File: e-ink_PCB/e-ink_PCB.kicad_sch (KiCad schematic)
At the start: 10 parts, among them J1 SEED C3, J2 e-ink-display, J3 SHT31, J4 100 uF CAP, J5 Batt Conn, Q1 FQP27P06

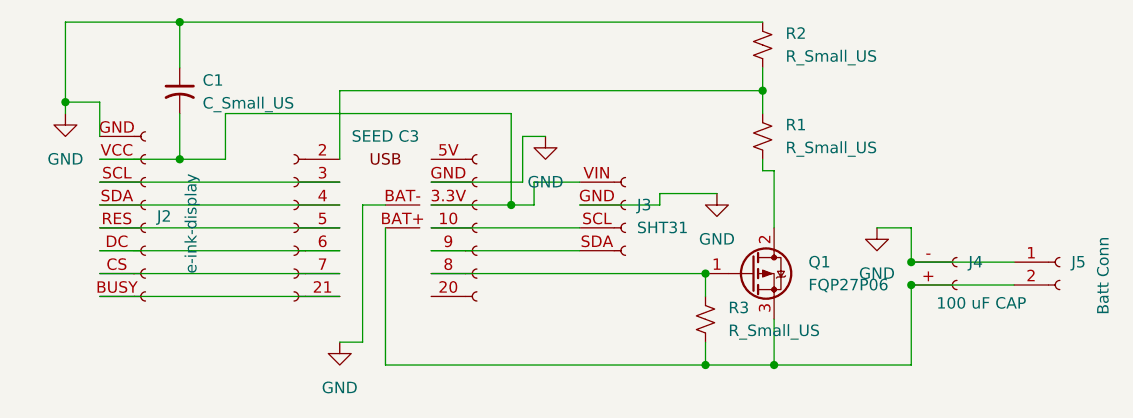
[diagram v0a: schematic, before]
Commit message: kiCAD correct display orientation
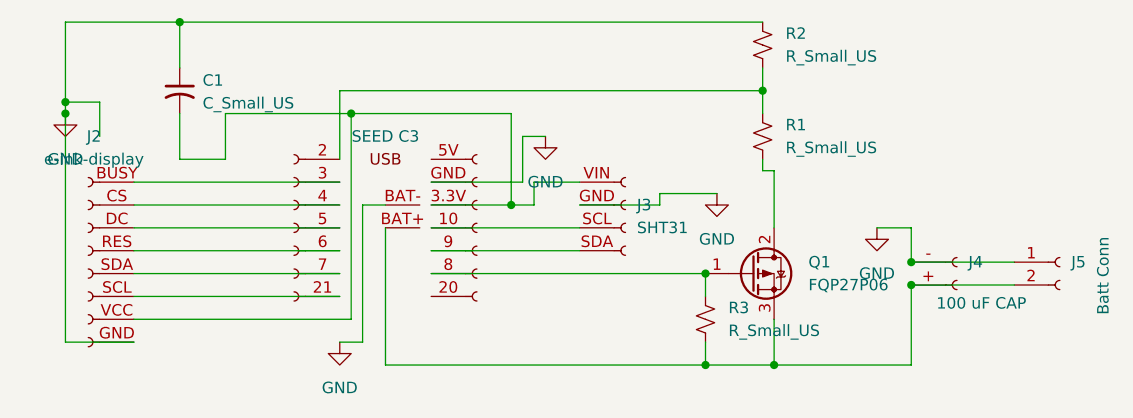
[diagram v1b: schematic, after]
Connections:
- net at J2.BUSY (Pin_8): now also J1.3 (Pin_7); no longer J1.21 (Pin_2)
- net at J2.CS (Pin_7): now also J1.4 (Pin_6); no longer J1.7 (Pin_3)
- net at J2.DC (Pin_6): now also J1.5 (Pin_5); no longer J1.6 (Pin_4)
- net at J2.RES (Pin_5): now also J1.6 (Pin_4); no longer J1.5 (Pin_5)
- net at J2.SCL (Pin_3): now also J1.21 (Pin_2); no longer J1.3 (Pin_7)
- net at J2.SDA (Pin_4): now also J1.7 (Pin_3); no longer J1.4 (Pin_6)
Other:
- moved on the sheet: J2
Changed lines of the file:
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@@
 	)
 	(junction
-		(at 72.39 72.39)
+		(at 91.44 67.31)
 		(diameter 0)
 		(color 0 0 0 0)
@@
 		(color 0 0 0 0)
 	)
-	(wire
-		(pts
-			(xy 77.47 72.39) (xy 72.39 72.39)
-		)
-		(stroke
-			(width 0)
-			(type default)
-		)
+	(junction
+		(at 59.69 67.31)
+		(diameter 0)
+		(color 0 0 0 0)
 	)
 	(wire
@@
 	(wire
 		(pts
+			(xy 67.31 85.09) (xy 90.17 85.09)
+		)
+		(stroke
+			(width 0)
+			(type default)
+		)
+	)
+	(wire
+		(pts
 			(xy 100.33 80.01) (xy 116.84 80.01)
 		)
@@
 	(wire
 		(pts
-			(xy 63.5 82.55) (xy 90.17 82.55)
+			(xy 72.39 72.39) (xy 77.47 72.39)
 		)
 		(stroke
@@
 	(wire
 		(pts
-			(xy 63.5 87.63) (xy 90.17 87.63)
+			(xy 67.31 87.63) (xy 90.17 87.63)
 		)
 		(stroke
@@
 	(wire
 		(pts
-			(xy 72.39 72.39) (xy 63.5 72.39)
+			(xy 67.31 82.55) (xy 90.17 82.55)
+		)
+		(stroke
+			(width 0)
+			(type default)
+		)
+	)
+	(wire
+		(pts
+			(xy 59.69 67.31) (xy 59.69 92.71)
+		)
+		(stroke
+			(width 0)
+			(type default)
+		)
+	)
+	(wire
+		(pts
+			(xy 67.31 92.71) (xy 59.69 92.71)
+		)
+		(stroke
+			(width 0)
+			(type default)
+		)
+	)
+	(wire
+		(pts
+			(xy 67.31 77.47) (xy 90.17 77.47)
 		)
 		(stroke
@@
 	(wire
 		(pts
+			(xy 91.44 67.31) (xy 77.47 67.31)
+		)
+		(stroke
+			(width 0)
+			(type default)
+		)
+	)
+	(wire
+		(pts
 			(xy 153.67 83.82) (xy 153.67 80.01)
 		)
@@
 	(wire
 		(pts
-			(xy 63.5 85.09) (xy 90.17 85.09)
-		)
-		(stroke
-			(width 0)
-			(type default)
-		)
-	)
-	(wire
-		(pts
 			(xy 100.33 85.09) (xy 130.81 85.09)
 		)
@@
 	(wire
 		(pts
+			(xy 67.31 74.93) (xy 90.17 74.93)
+		)
+		(stroke
+			(width 0)
+			(type default)
+		)
+	)
+	(wire
+		(pts
 			(xy 137.16 64.77) (xy 137.16 67.31)
 		)
@@
 	(wire
 		(pts
-			(xy 63.5 77.47) (xy 90.17 77.47)
-		)
-		(stroke
-			(width 0)
-			(type default)
-		)
-	)
-	(wire
-		(pts
-			(xy 109.22 67.31) (xy 77.47 67.31)
+			(xy 109.22 67.31) (xy 91.44 67.31)
 		)
 		(stroke
@@
 	(wire
 		(pts
-			(xy 63.5 74.93) (xy 90.17 74.93)
-		)
-		(stroke
-			(width 0)
-			(type default)
-		)
-	)
-	(wire
-		(pts
 			(xy 59.69 57.15) (xy 59.69 66.04)
 		)
@@
 	(wire
 		(pts
+			(xy 91.44 67.31) (xy 91.44 90.17)
+		)
+		(stroke
+			(width 0)
+			(type default)
+		)
+	)
+	(wire
+		(pts
 			(xy 125.73 77.47) (xy 116.84 77.47)
 		)
@@
 	(wire
 		(pts
+			(xy 67.31 80.01) (xy 90.17 80.01)
+		)
+		(stroke
+			(width 0)
+			(type default)
+		)
+	)
+	(wire
+		(pts
+			(xy 91.44 90.17) (xy 67.31 90.17)
+		)
+		(stroke
+			(width 0)
+			(type default)
+		)
+	)
+	(wire
+		(pts
 			(xy 72.39 67.31) (xy 72.39 72.39)
 		)
@@
 		(pts
 			(xy 109.22 77.47) (xy 100.33 77.47)
-		)
-		(stroke
-			(width 0)
-			(type default)
-		)
-	)
-	(wire
-		(pts
-			(xy 63.5 80.01) (xy 90.17 80.01)
 		)
 		(stroke
@@
 	(symbol
 		(lib_id "Connector:Conn_01x09_Socket")
-		(at 68.58 80.01 0)
+		(at 62.23 82.55 180)
 		(unit 1)
 		(exclude_from_sim no)
@@
 		(fields_autoplaced yes)
 		(property "Reference" "J2"
-			(at 69.85 78.7399 0)
-			(effects
-				(font
-					(size 1.27 1.27)
-				)
-				(justify left)
+			(at 62.865 69.85 0)
+			(effects
+				(font
+					(size 1.27 1.27)
+				)
 			)
 		)
 		(property "Value" "e-ink-display"
-			(at 73.66 85.09 90)
-			(effects
-				(font
-					(size 1.27 1.27)
-				)
-				(justify left)
+			(at 62.865 72.39 0)
+			(effects
+				(font
+					(size 1.27 1.27)
+				)
 			)
 		)
 		(property "Footprint" "Connector_PinHeader_2.54mm:PinHeader_1x08_P2.54mm_Vertical"
-			(at 68.58 80.01 0)
+			(at 62.23 82.55 0)
 			(effects
 				(font
@@
 		)
 		(property "Datasheet" "~"
-			(at 68.58 80.01 0)
+			(at 62.23 82.55 0)
 			(effects
 				(font
@@
 		)
 		(property "Description" "Generic connector, single row, 01x09, script generated"
-			(at 68.58 80.01 0)
-			(effects
-				(font
+			(at 62.23 82.55 0)
+			(effects
+				(font
